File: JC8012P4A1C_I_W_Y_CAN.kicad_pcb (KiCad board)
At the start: 2 copper layers, 66 x 54 mm, 31 parts, among them J1 610110249121, J2 68711414522, J3 653104131822, Q1 DMP6050SSD, U1 TLE9250VSJ, U2 171030601

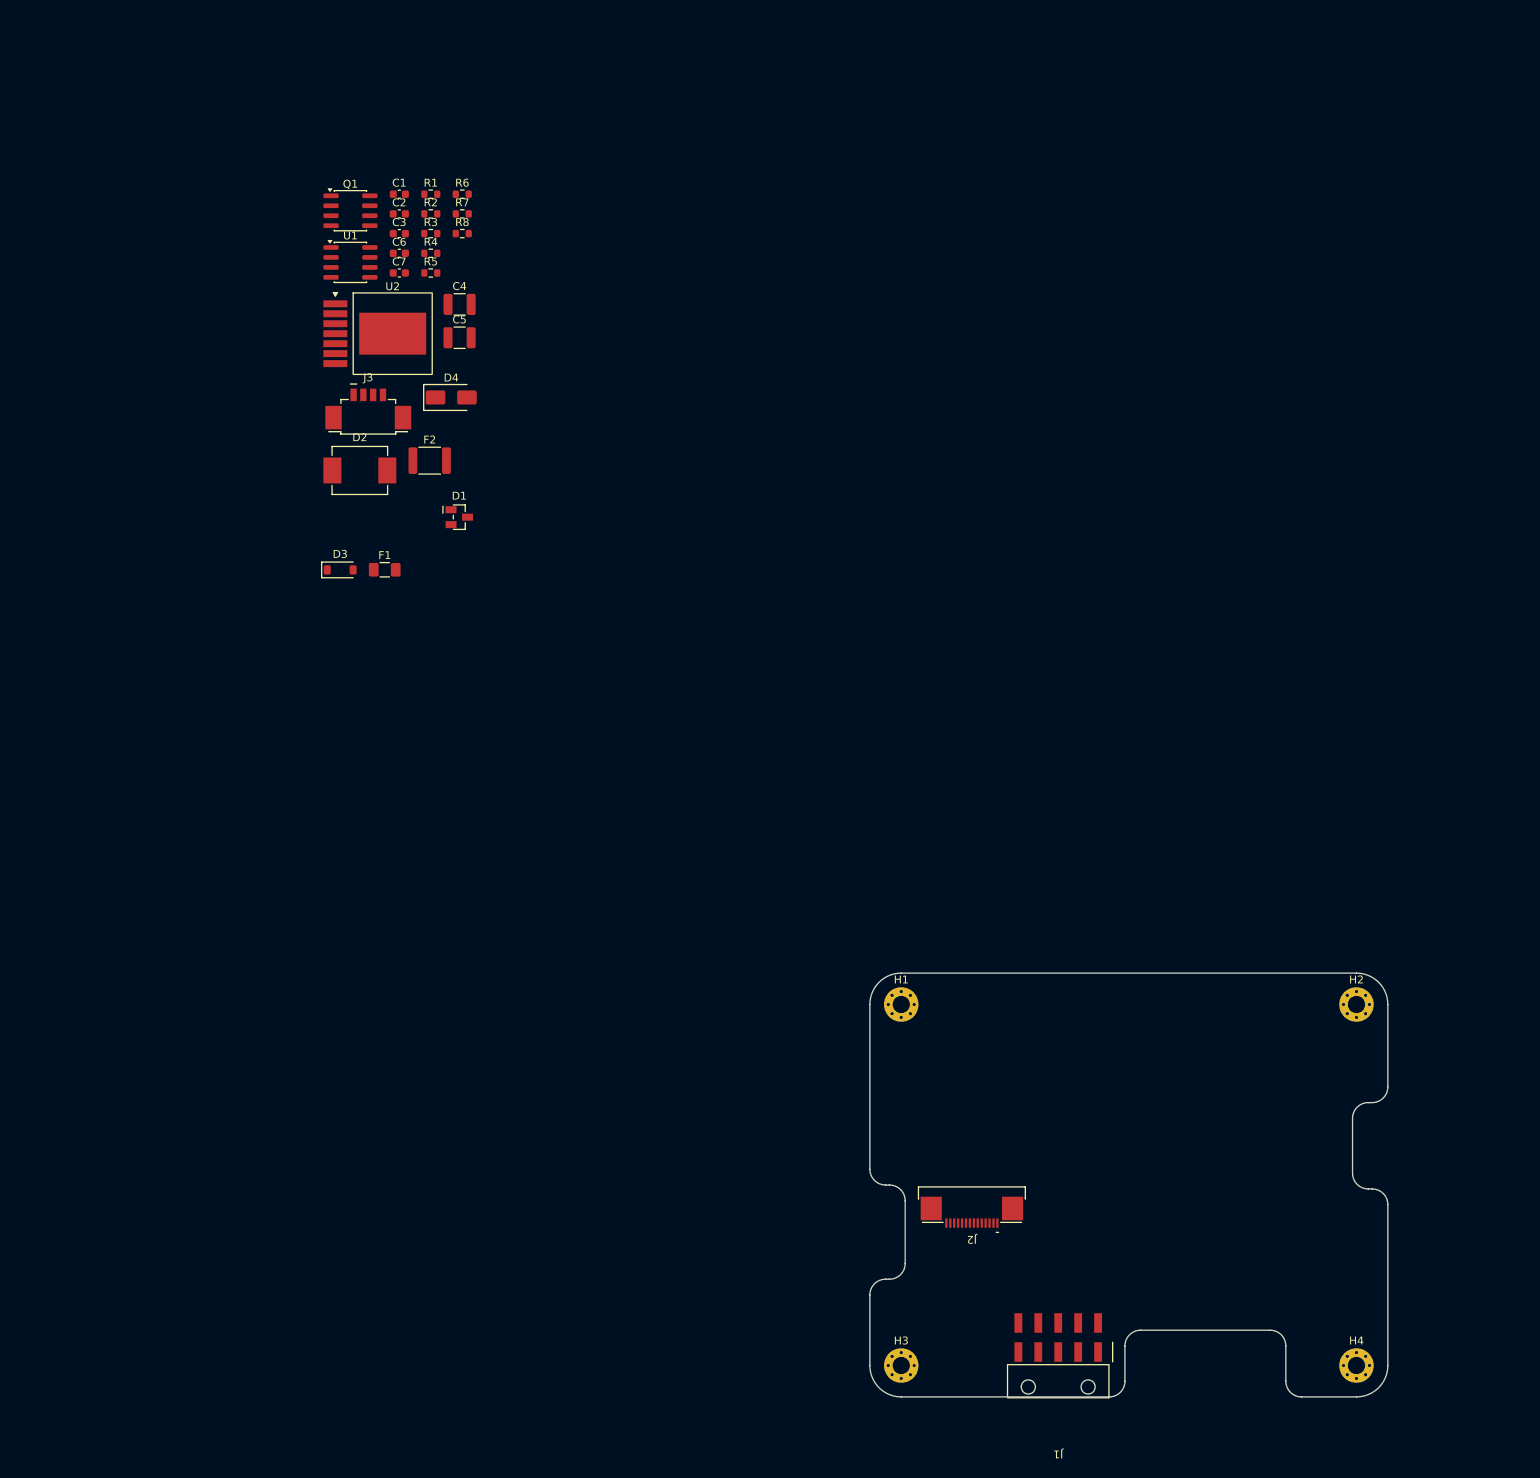
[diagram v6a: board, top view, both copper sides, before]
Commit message: Power supply on its own sheet, EMI filter, UVLO, part numbers
Schematic:
- New hierarchical sheet "Versorgung" (power.kicad_sch) with input
  protection, EMI filter, buck converter and TBC supply; connected to
  the main sheet by global labels ECU_PWR_IN, TBC_PWR_OUT, +5V, GND.
  Netlist checked: same parts and connections as before the split.
- Input EMI filter as recommended in the 171030601 datasheet (p. 47,
  EN55022 class B): C8 1 uF (885012209047) + L2 10 uH WE-PD2 (74477410)
- C9 47 uF/50 V SMD electrolytic (865080649013, D8 x 6.5 mm) damping
  the input, behind the reverse polarity protection
- Second input MLCC C12 10 uF/50 V X7R (datasheet: >= 10 uF after
  derating), output C5/C11 2 x 47 uF/10 V X5R + C10 220 uF polymer
  (875105244013), as on the Wuerth evaluation board
- UVLO divider R9 57k6 / R10 10k: on at ~8.0 V, off at ~7.4 V,
  EN stays below 6.5 V up to the 38.9 V TVS clamp voltage
- Wuerth part numbers (MPN, manufacturer, datasheet) on all
  capacitors and L2. Several Wuerth KiCad library symbols carry a
  wrong Value/Footprint (shifted to the neighbour part); the values
  and footprints were taken from the datasheets instead.

Board:
- Footprints of the new parts imported (not placed yet), orphaned
  footprints from before the sheet split removed

Co-Authored-By: Claude Opus 5.5 <noreply@anthropic.com>
Claude-Session: https://claude.ai/code/session_014h8cGi8SRWthYdGFH1Qgzz
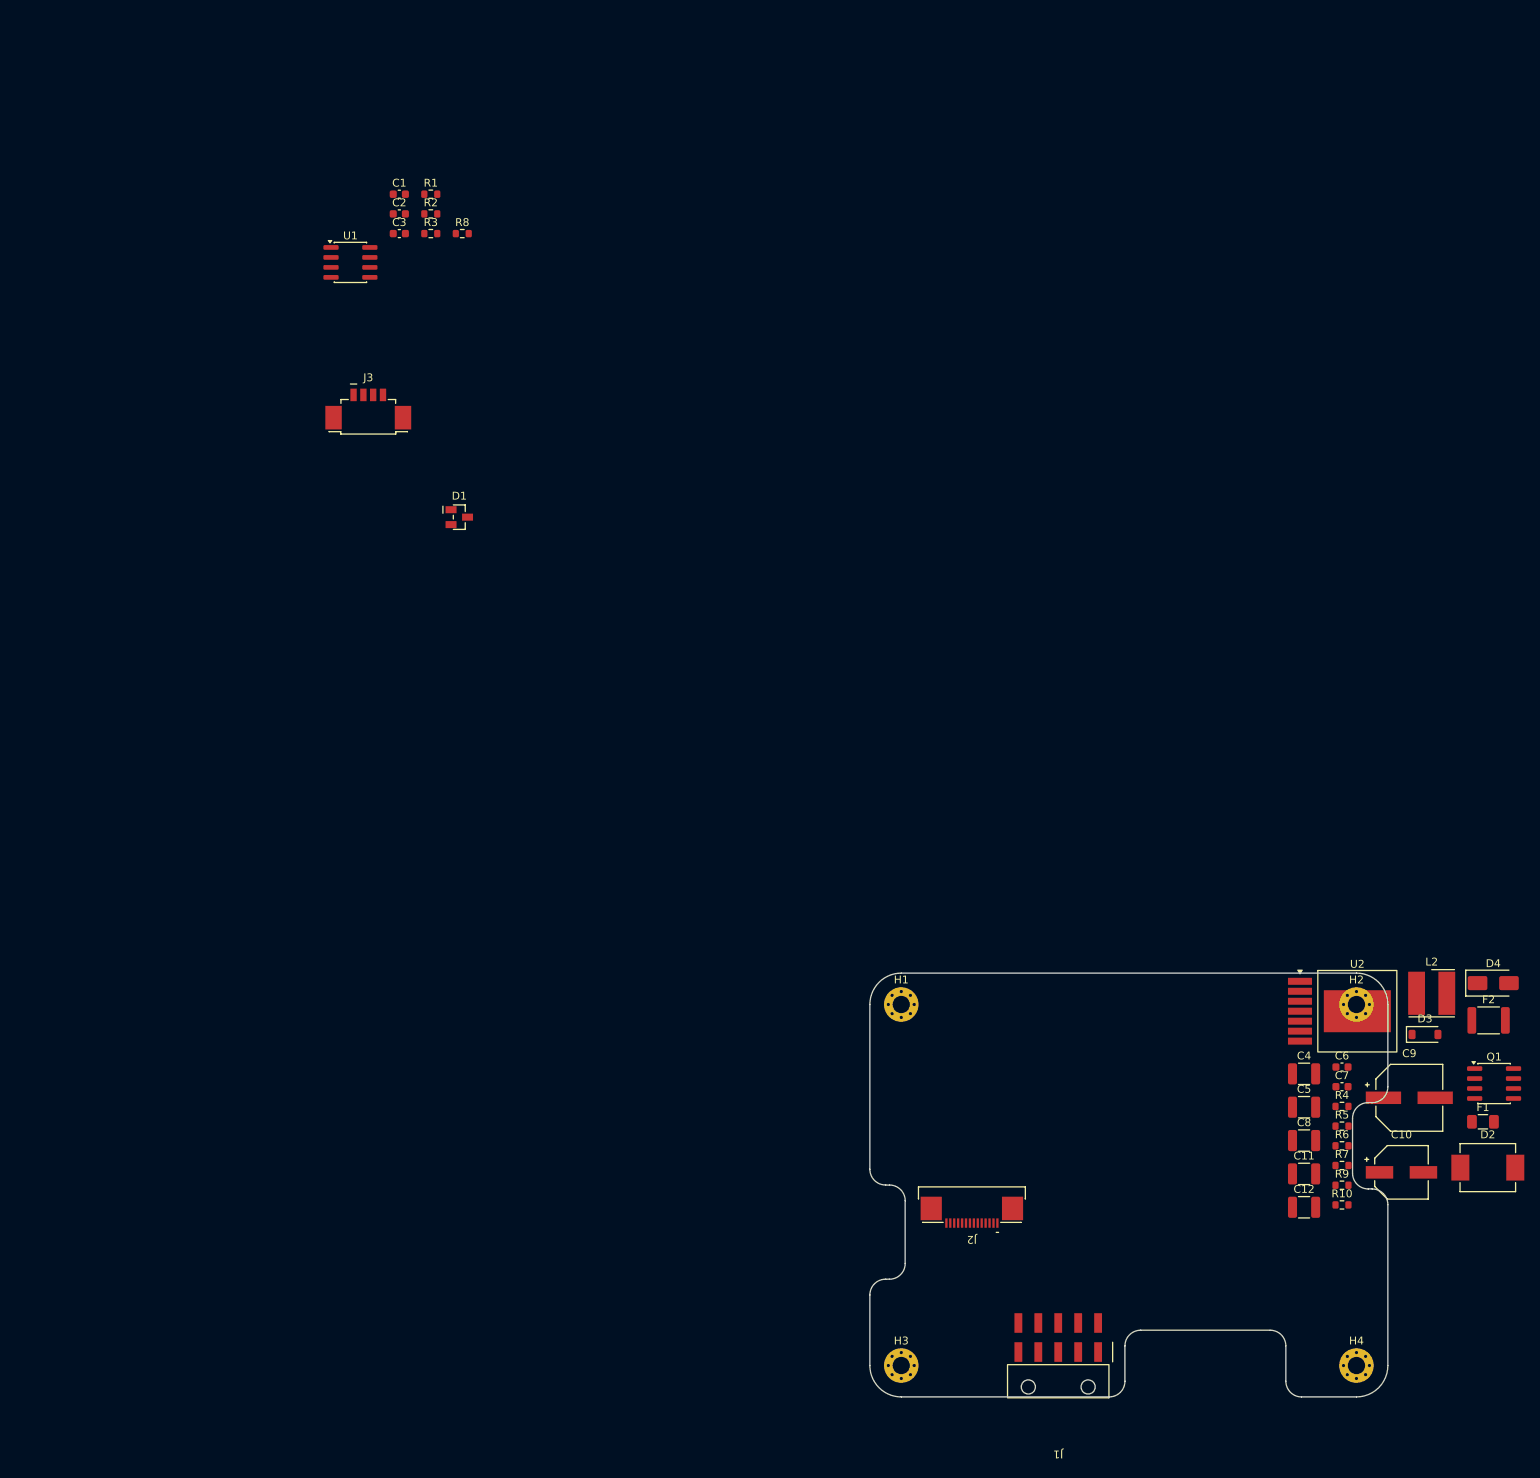
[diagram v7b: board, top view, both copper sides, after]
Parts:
- added C10: 220u/10V, JC8012P4A1C_CAN:CP_Wurth_WCAP-PSLP-D6.3L5.8, F.Cu at (167.7, 125.4)
- added C11: 47u/10V, Capacitor_SMD:C_1210_3225Metric, F.Cu at (155.3, 125.6)
- added C12: 10u/50V, Capacitor_SMD:C_1210_3225Metric, F.Cu at (155.3, 129.8)
- added C8: 1u/50V, Capacitor_SMD:C_1210_3225Metric, F.Cu at (155.3, 121.3)
- added C9: 47u/50V, JC8012P4A1C_CAN:CP_Wurth_WCAP-ASLI-D8L6.5, F.Cu at (168.7, 115.9)
- added L2: 10uH, JC8012P4A1C_CAN:L_Wurth_WE-PD2-5848, F.Cu at (171.6, 102.6)
- added R10: 10k 1%, Resistor_SMD:R_0603_1608Metric, F.Cu at (160.2, 129.5)
- added R9: 57k6 1%, Resistor_SMD:R_0603_1608Metric, F.Cu at (160.2, 127.0)
- C5: value 100u/10V -> 47u/10V
- moved Q1 183.3 mm to (179.5, 114.1)
- moved D2 169.0 mm to (178.7, 124.8)
- moved R6 165.1 mm to (160.2, 122.0)
- moved R7 165.1 mm to (160.2, 124.5)
- moved R4 159.0 mm to (160.2, 117.0)
- moved R5 159.0 mm to (160.2, 119.5)
- moved C6 158.7 mm to (160.2, 112.0)
- moved C7 158.7 mm to (160.2, 114.5)
- moved F1 156.6 mm to (178.1, 118.9)
- moved F2 152.6 mm to (178.8, 106.0)
- moved D4 152.3 mm to (179.4, 101.3)
- moved D3 150.4 mm to (170.7, 107.8)
- moved U2 150.2 mm to (162.1, 104.9)
- moved C4 145.6 mm to (155.3, 112.8)
- moved C5 145.6 mm to (155.3, 117.1)
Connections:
- net /+5V renamed +5V
- net /BUCK_FB renamed /Versorgung/BUCK_FB
- net /BUCK_RON renamed /Versorgung/BUCK_RON
- net /BUCK_SS renamed /Versorgung/BUCK_SS
- net /ECU_PWR renamed /Versorgung/ECU_PWR
- net /ECU_PWR_IN renamed ECU_PWR_IN
- net /GND renamed GND
- net /PFET_G renamed /Versorgung/PFET_G
- net /TBC_PWR_OUT renamed TBC_PWR_OUT
- C4 pad 1: /VIN_PROT -> /Versorgung/VIN_BUCK
- D3 pad 1: /VIN_PROT -> /Versorgung/VIN_PROT
- D4 pad 2: /VIN_PROT -> /Versorgung/VIN_PROT
- Q1 pad 1: /VIN_PROT -> /Versorgung/VIN_PROT
- Q1 pad 3: /VIN_PROT -> /Versorgung/VIN_PROT
- R5 pad 1: /VIN_PROT -> /Versorgung/VIN_BUCK
- U2 pad 1: /VIN_PROT -> /Versorgung/VIN_BUCK
- U2 pad 3: unconnected-(U2-EN-Pad3) -> /Versorgung/BUCK_EN

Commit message: Part numbers for all remaining parts, Q1 -> Si4948BEY
- Resistors Yageo RC series 1 %. R1/R2 (split termination 750R) in
  1206 / 0.25 W: ISO 11783-2 asks for >= 125 mW for the termination
  resistors; worst case (CAN_H shorted to 24 V) is ~0.19 W each.
- D3 onsemi MMSZ5245BT1G (15 V), D4 Diodes B160-13-F (60 V Schottky)
- F1 Littelfuse 0452001.MRL NANO2 Slo-Blo 1 A / 125 V (1206 slow fuses
  are only rated 32-63 V), footprint changed to NANO2
- F2 Bourns MF-MSMF014-2 (PTC 0.14 A / 60 V, 1812)
- Q1 Vishay SI4948BEY-T1-E3 instead of the unavailable DMP6050SSD:
  dual P-ch 60 V, same SO-8 pinout (S1 G1 S2 G2 D2 D2 D1 D1), both
  halves in parallel (~60 mOhm)
- U1 Infineon TLE9250VSJXUMA1
- Every part now has MPN and manufacturer fields
- Board updated with F8 (new footprints for R1/R2/F1)

Part numbers derived from the manufacturers' naming schemes; check
availability with the Mouser BOM import before ordering.

Co-Authored-By: Claude Opus 5.5 <noreply@anthropic.com>
Claude-Session: https://claude.ai/code/session_014h8cGi8SRWthYdGFH1Qgzz
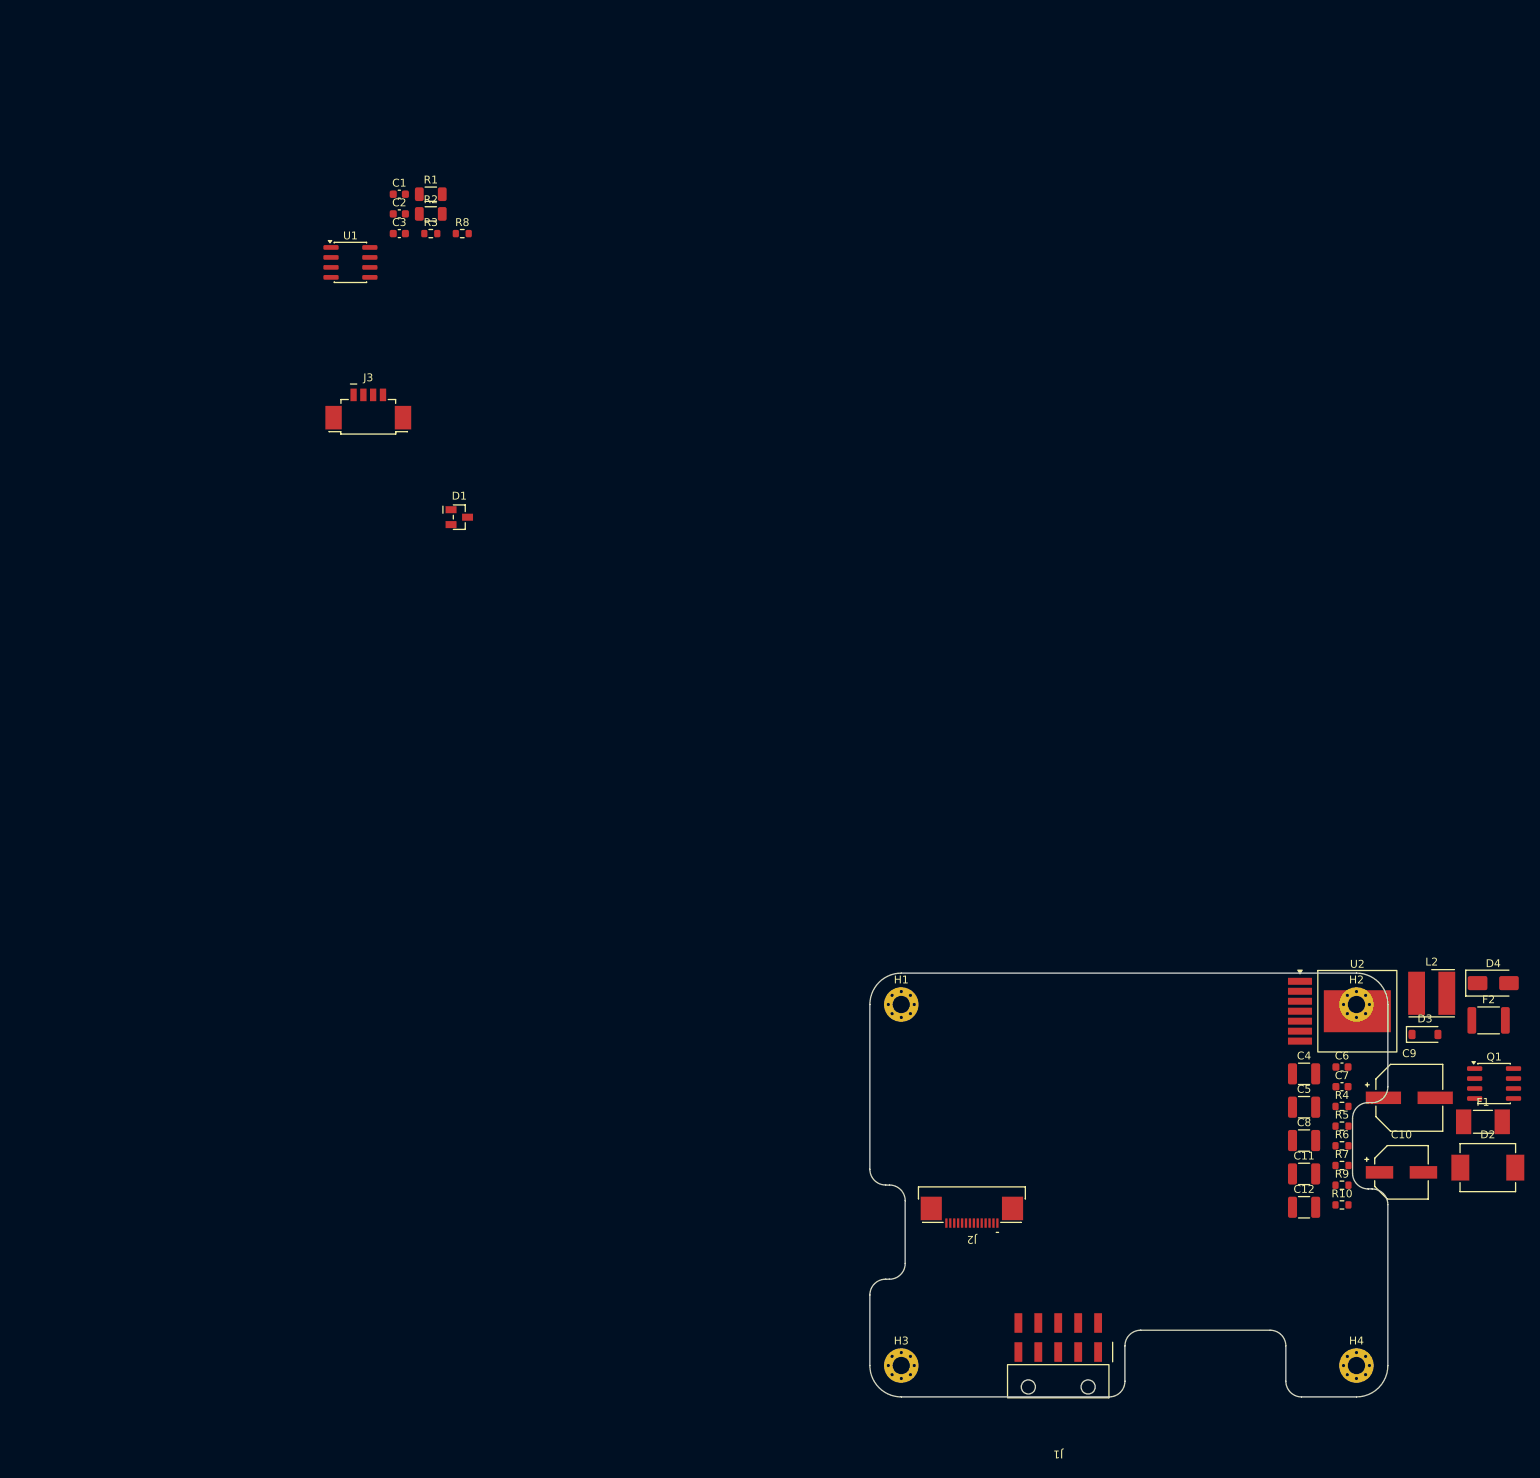
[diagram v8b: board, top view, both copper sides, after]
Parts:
- D4: value SS16 -> B160
- F1: value 1A slow -> 1A slow 125V; footprint Fuse:Fuse_1206_3216Metric -> Fuse:Fuse_Littelfuse-NANO2-451_453
- Q1: value DMP6050SSD -> Si4948BEY
- R1, R2: value 750 -> 750 1%; footprint Resistor_SMD:R_0603_1608Metric -> Resistor_SMD:R_1206_3216Metric
- R3: value 10k -> 10k 1%
- R4, R5: value 100k -> 100k 1%
- R6: value 5k62 -> 5k62 1%
- R7: value 1k07 -> 1k07 1%
